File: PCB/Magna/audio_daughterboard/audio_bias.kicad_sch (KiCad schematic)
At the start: 8 parts, among them U801 NE5532

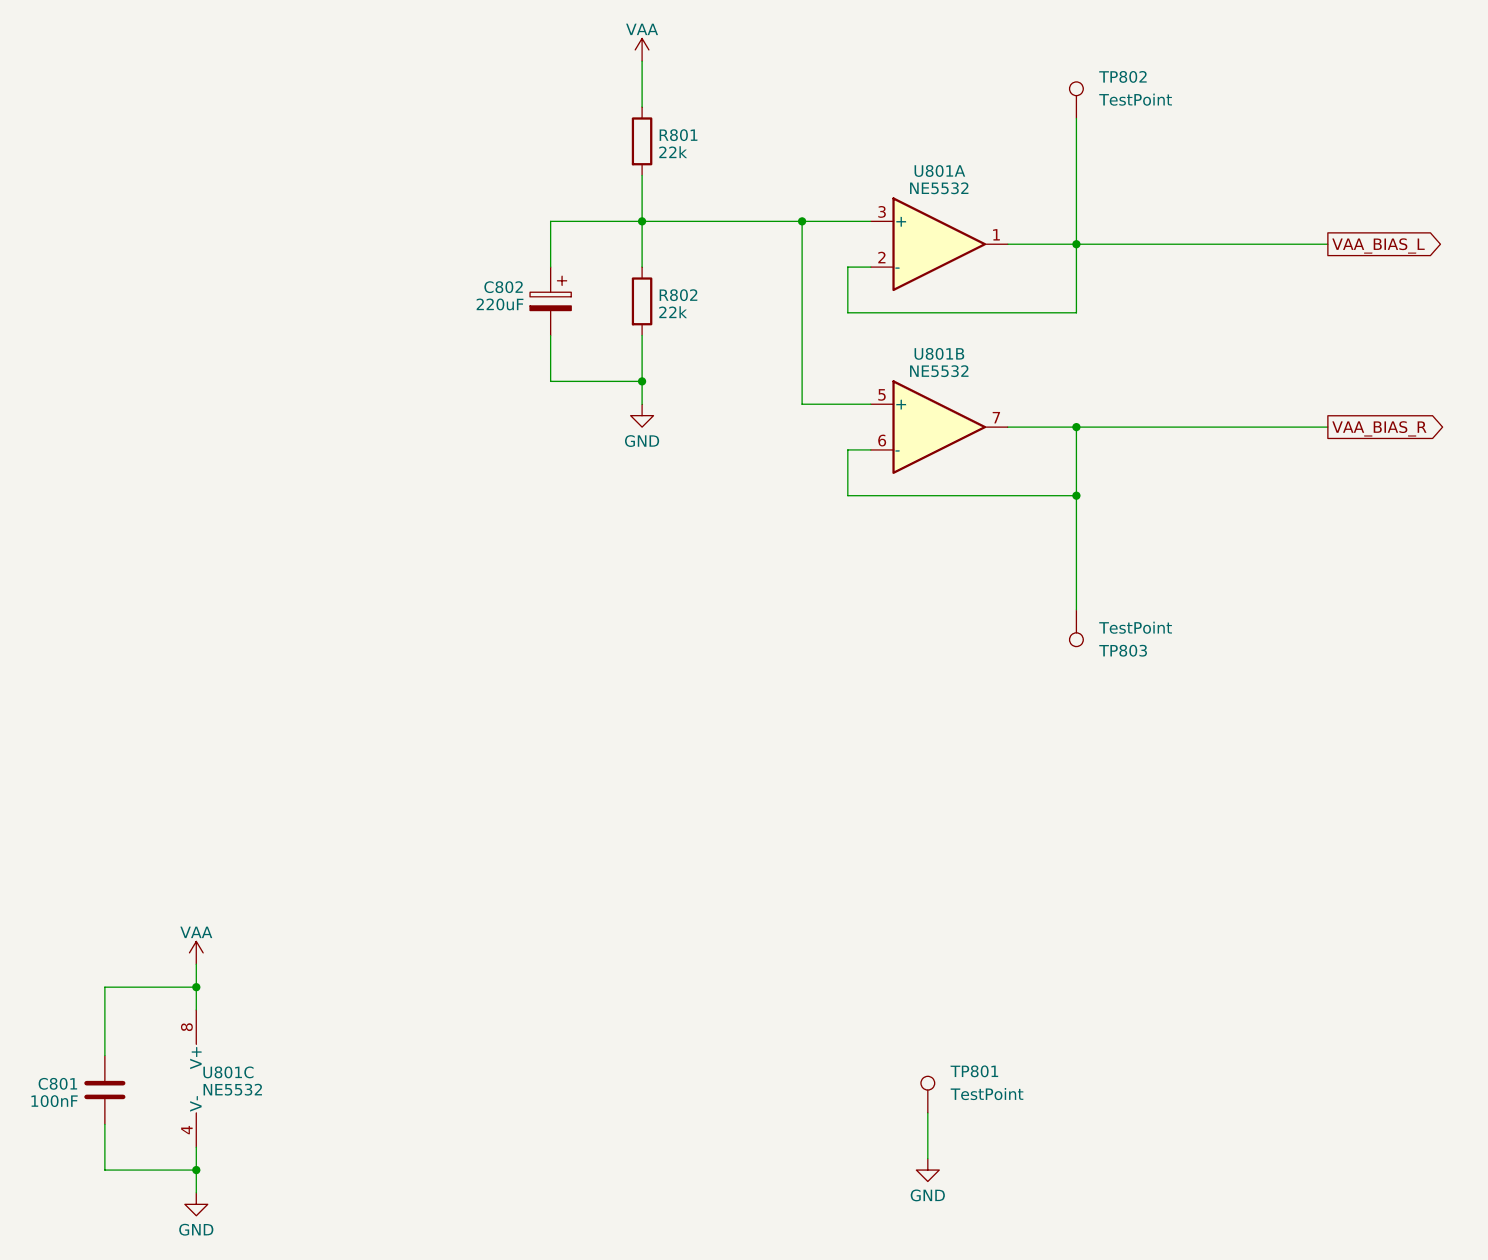
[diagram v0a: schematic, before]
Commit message: "Finalize" Audio daugherboard
Finished DAC output filter
Fixed the whole damn MCU subschematic
Fixed Linedriver schematic
Added component footprints and LCSC numbers
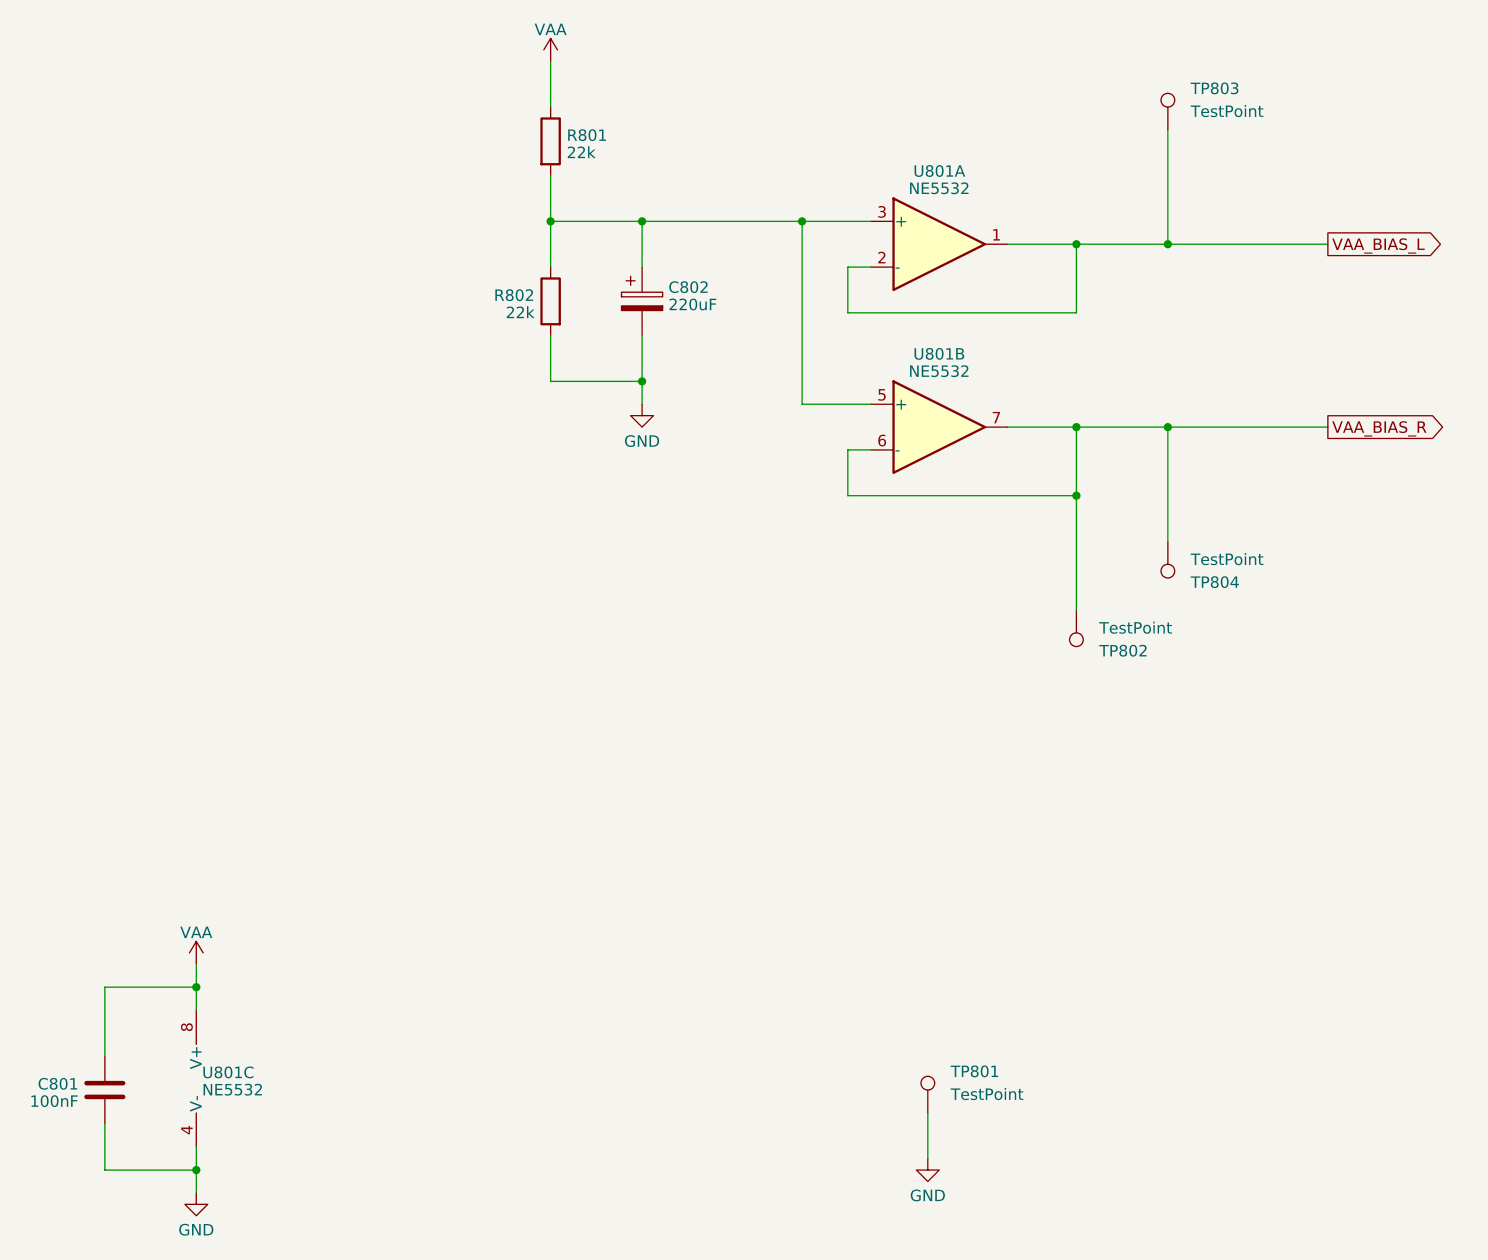
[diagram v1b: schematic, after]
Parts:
- added TP804: TestPoint, TestPoint:TestPoint_Keystone_5005-5009_Compact, symbol Connector:TestPoint
- C801, C802, TP801, U801: now left out of the parts list
- R801, R802: footprint Resistor_SMD:R_0805_2012Metric_Pad1.20x1.40mm_HandSolder -> Resistor_SMD:R_0603_1608Metric; LCSC C479095 -> C335085; now left out of the parts list
- TP802: renamed from TP803; now left out of the parts list
- TP803: renamed from TP802; now left out of the parts list
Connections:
- net VAA_BIAS_R: now also TP804.1
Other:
- moved on the sheet: C802, R801, R802, TP803

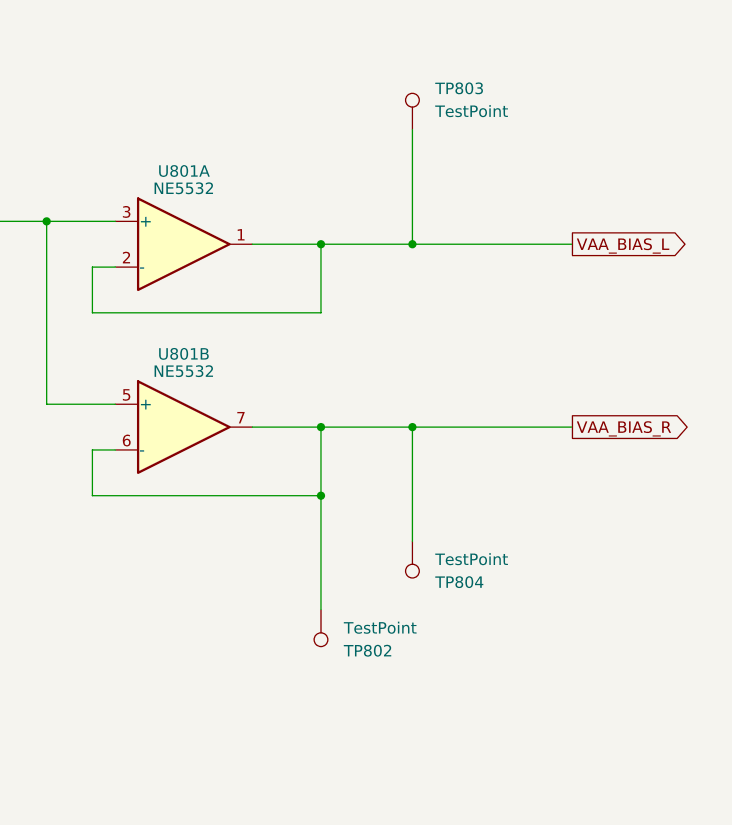
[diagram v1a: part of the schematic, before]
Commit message: Do most of the component placement for audio board
Just a general layout, things will probably change
as the routing begins.
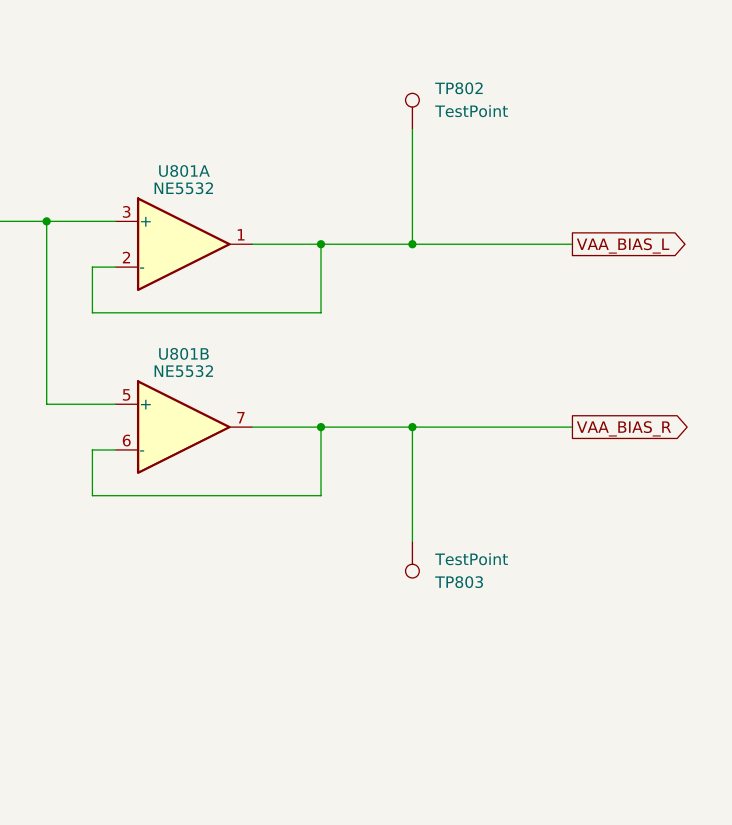
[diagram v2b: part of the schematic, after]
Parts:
- removed TP802: TestPoint, TestPoint:TestPoint_Keystone_5005-5009_Compact, symbol Connector:TestPoint
- C801: footprint Capacitor_SMD:C_0805_2012Metric_Pad1.18x1.45mm_HandSolder -> Capacitor_SMD:C_0603_1608Metric; LCSC C49678 -> C14663
- C802: LCSC C2165067 -> C729680
- renumbered TP803 to TP802, TP804 to TP803
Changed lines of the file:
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@@
-	)
-	(junction
-		(at 158.75 105.41)
-		(diameter 0)
-		(color 0 0 0 0)
 	)
 	(junction
@@
 		(pts
 			(xy 133.35 85.09) (xy 158.75 85.09)
-		)
-		(stroke
-			(width 0)
-			(type default)
-		)
-	)
-	(wire
-		(pts
-			(xy 158.75 118.11) (xy 158.75 105.41)
 		)
 		(stroke
@@
 		(dnp no)
 		(fields_autoplaced yes)
-		(property "Reference" "TP804"
+		(property "Reference" "TP803"
 			(at 171.45 115.062 0)
 			(effects
@@
 				)
 				(hide yes)
+			)
+		)
+		(property "Field5" ""
+			(at 168.91 110.49 0)
+			(effects
+				(font
+					(size 1.27 1.27)
+				)
 			)
 		)
@@
 			(project "Audio_daughterboard"
 				(path "/1eadd930-2484-4c28-b568-78e6454e7f52/eddc896c-2eca-4cc9-a7eb-0b3af1aefe11"
-					(reference "TP804")
+					(reference "TP803")
 					(unit 1)
 				)
@@
 			)
 		)
+		(property "Field5" ""
+			(at 100.33 66.04 0)
+			(effects
+				(font
+					(size 1.27 1.27)
+				)
+			)
+		)
 		(pin "1"
 		)
@@
 			)
 		)
+		(property "Field5" ""
+			(at 143.51 97.79 0)
+			(effects
+				(font
+					(size 1.27 1.27)
+				)
+			)
+		)
 		(pin "1"
 		)
@@
 			)
 		)
+		(property "Field5" ""
+			(at 63.5 170.18 0)
+			(effects
+				(font
+					(size 1.27 1.27)
+				)
+			)
+		)
 		(pin "1"
 		)
@@
 				)
 				(hide yes)
+			)
+		)
+		(property "Field5" ""
+			(at 143.51 77.47 0)
+			(effects
+				(font
+					(size 1.27 1.27)
+				)
 			)
 		)
@@
 			)
 		)
+		(property "Field5" ""
+			(at 100.33 83.82 0)
+			(effects
+				(font
+					(size 1.27 1.27)
+				)
+			)
+		)
 		(pin "1"
 		)
@@
 			)
 		)
+		(property "Field5" ""
+			(at 142.24 173.99 0)
+			(effects
+				(font
+					(size 1.27 1.27)
+				)
+			)
+		)
 		(pin "1"
 		)
@@
 				(path "/1eadd930-2484-4c28-b568-78e6454e7f52/eddc896c-2eca-4cc9-a7eb-0b3af1aefe11"
 					(reference "TP801")
-					(unit 1)
-				)
-			)
-		)
-	)
-	(symbol
-		(lib_id "Connector:TestPoint")
-		(at 158.75 118.11 0)
-		(mirror x)
-		(unit 1)
-		(exclude_from_sim yes)
-		(in_bom no)
-		(on_board yes)
-		(dnp no)
-		(fields_autoplaced yes)
-		(property "Reference" "TP802"
-			(at 161.29 122.682 0)
-			(effects
-				(font
-					(size 1.27 1.27)
-				)
-				(justify left)
-			)
-		)
-		(property "Value" "TestPoint"
-			(at 161.29 120.142 0)
-			(effects
-				(font
-					(size 1.27 1.27)
-				)
-				(justify left)
-			)
-		)
-		(property "Footprint" "TestPoint:TestPoint_Keystone_5005-5009_Compact"
-			(at 163.83 118.11 0)
-			(effects
-				(font
-					(size 1.27 1.27)
-				)
-				(hide yes)
-			)
-		)
-		(property "Datasheet" "~"
-			(at 163.83 118.11 0)
-			(effects
-				(font
-					(size 1.27 1.27)
-				)
-				(hide yes)
-			)
-		)
-		(property "Description" "test point"
-			(at 158.75 118.11 0)
-			(effects
-				(font
-					(size 1.27 1.27)
-				)
-				(hide yes)
-			)
-		)
-		(pin "1"
-		)
-		(instances
-			(project "Magna"
-				(path "/1469ea1f-a157-49dc-a369-2d42fa17695d/22259812-9e7f-4230-9f2b-a9eb5ce4aaf1/eddc896c-2eca-4cc9-a7eb-0b3af1aefe11"
-					(reference "TP?")
-					(unit 1)
-				)
-			)
-			(project "Audio_daughterboard"
-				(path "/1eadd930-2484-4c28-b568-78e6454e7f52/eddc896c-2eca-4cc9-a7eb-0b3af1aefe11"
-					(reference "TP802")
 					(unit 1)
 				)
@@
 			)
 		)
-		(property "LCSC" "C2165067"
+		(property "LCSC" "C729680"
 			(at 110.49 83.82 90)
 			(effects
@@
 				)
 				(hide yes)
+			)
+		)
+		(property "Field5" ""
+			(at 110.49 83.82 0)
+			(effects
+				(font
+					(size 1.27 1.27)
+				)
 			)
 		)
@@
 		(dnp no)
 		(fields_autoplaced yes)
-		(property "Reference" "TP803"
+		(property "Reference" "TP802"
 			(at 171.45 60.198 0)
 			(effects
@@
 				)
 				(hide yes)
+			)
+		)
+		(property "Field5" ""
+			(at 168.91 64.77 0)
+			(effects
+				(font
+					(size 1.27 1.27)
+				)
 			)
 		)
@@
 			(project "Audio_daughterboard"
 				(path "/1eadd930-2484-4c28-b568-78e6454e7f52/eddc896c-2eca-4cc9-a7eb-0b3af1aefe11"
-					(reference "TP803")
+					(reference "TP802")
 					(unit 1)
 				)
@@
 			)
 		)
-		(property "Footprint" "Capacitor_SMD:C_0805_2012Metric_Pad1.18x1.45mm_HandSolder"
+		(property "Footprint" "Capacitor_SMD:C_0603_1608Metric"
 			(at 49.8348 175.26 0)
 			(effects
@@
 			)
 		)
-		(property "LCSC" "C49678"
+		(property "LCSC" "C14663"
 			(at 50.8 171.45 0)
 			(effects
@@
 			)
 		)
+		(property "Field5" ""
+			(at 50.8 171.45 0)
+			(effects
+				(font
+					(size 1.27 1.27)
+				)
+			)
+		)
